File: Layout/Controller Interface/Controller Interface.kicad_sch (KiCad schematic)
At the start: 19 parts, among them J1 Conn_01x05_Socket, J2 Conn_01x05_Socket, J3 Conn_01x05_Socket, J4 Conn_01x05_Socket, Q1 FFB3904, Q3 FFB3904, SW1 SW_Push, SW2 SW_Push, U1 NRF24L01_Breakout, U2 Pico, U3 LD1117V33

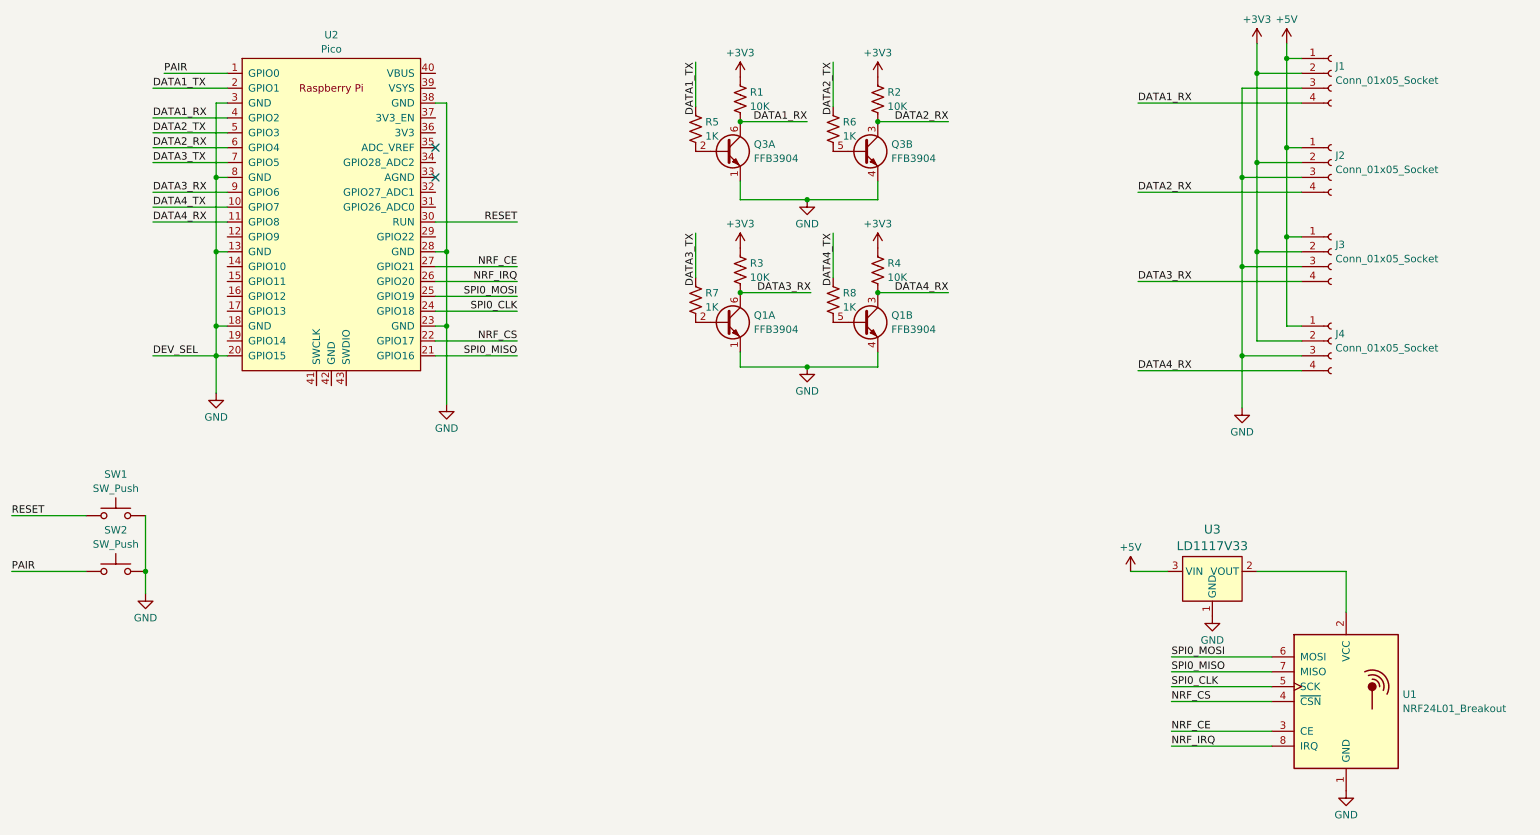
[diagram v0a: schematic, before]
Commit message: Refactor rx/tx PIO into single program
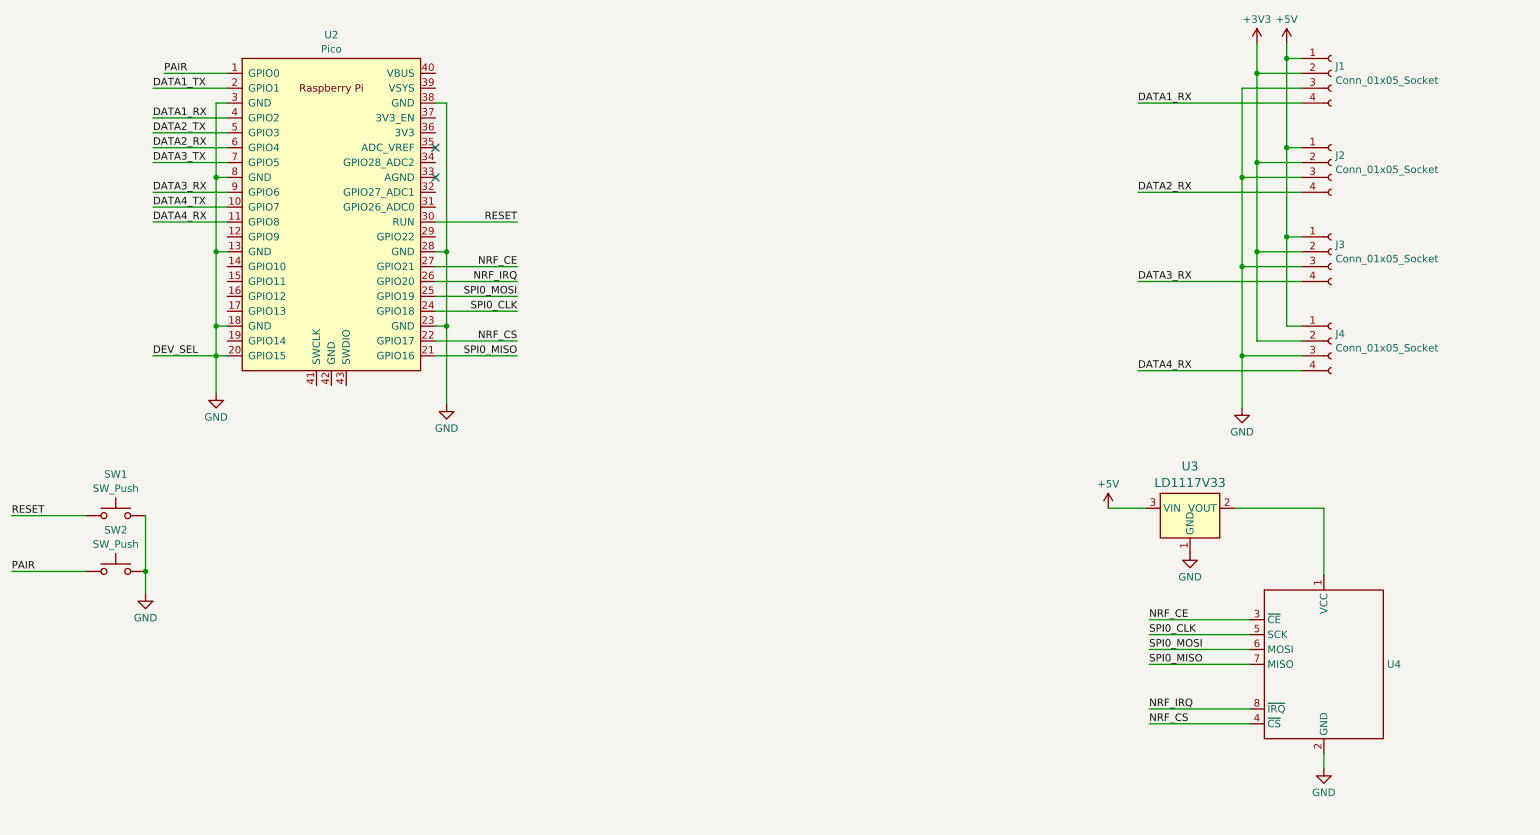
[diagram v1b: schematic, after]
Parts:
- removed Q1, Q3: FFB3904, Package_TO_SOT_SMD:SOT-363_SC-70-6, symbol Transistor_BJT:FFB3904
- removed R1, R2, R3, R4: 10K, symbol Device:R_US
- removed R5, R6, R7, R8: 1K, symbol Device:R_US
- removed U1: NRF24L01_Breakout, RF_Module:nRF24L01_Breakout, symbol RF:NRF24L01_Breakout
- added U4: ~, symbol RF:NRF24L01_Mini
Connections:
- net GND: now also U4.2 (GND)
- net NRF_CE: now also U4.3 (~{CE})
- net NRF_CS: now also U4.4 (~{CS})
- net NRF_IRQ: now also U4.8 (~{IRQ})
- net SPI0_CLK: now also U4.5 (SCK)
- net SPI0_MISO: now also U4.7 (MISO)
- net SPI0_MOSI: now also U4.6 (MOSI)
- net at U3.2 (VOUT): now also U4.1 (VCC)
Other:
- moved on the sheet: U3

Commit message: More work on the controller layout
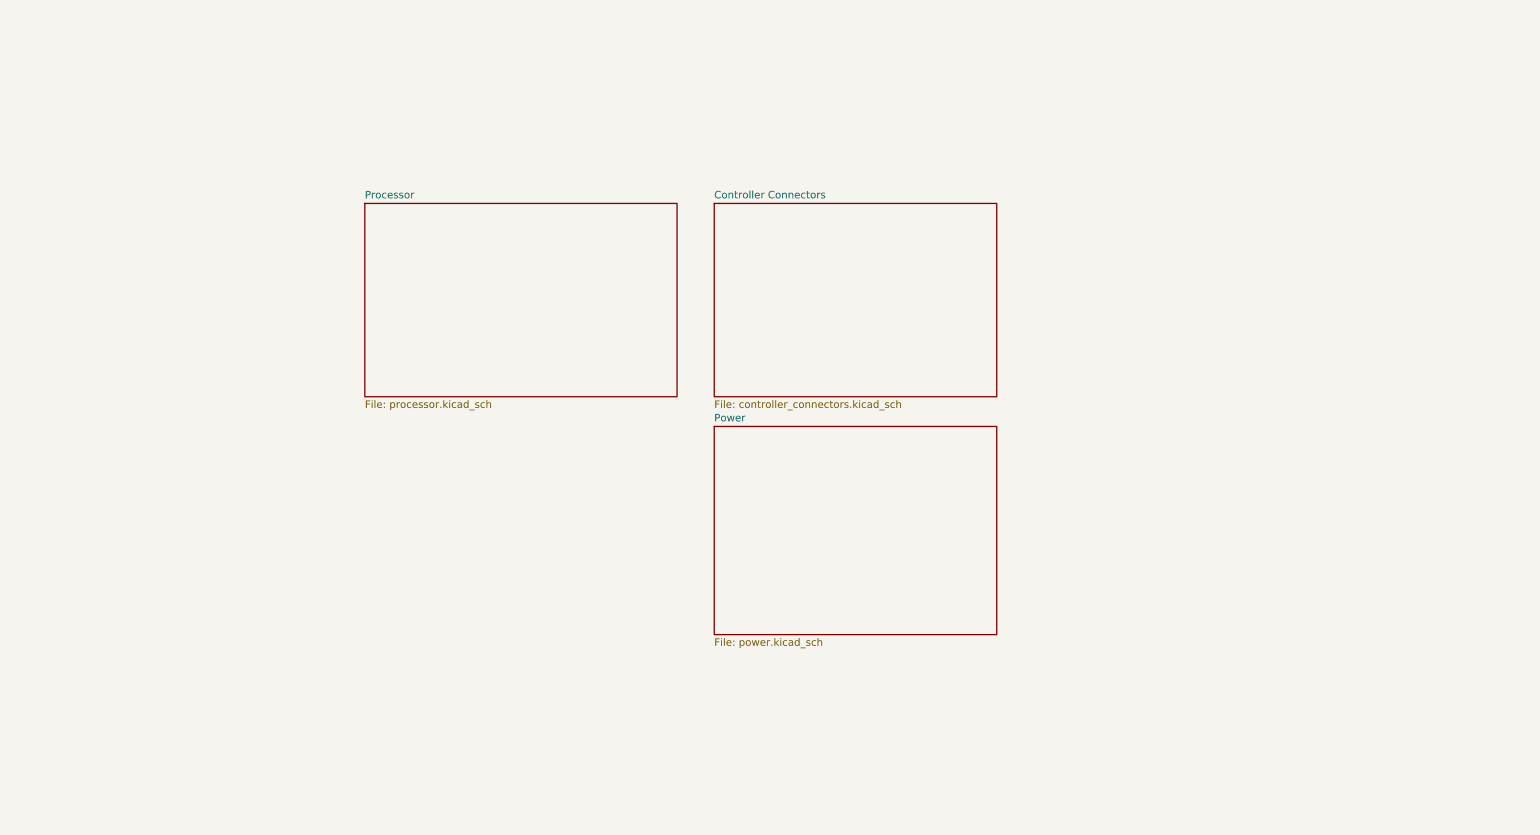
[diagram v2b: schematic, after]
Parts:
- removed J1, J2, J3, J4: Conn_01x05_Socket, symbol Connector:Conn_01x04_Socket
- removed SW1, SW2: SW_Push, symbol Switch:SW_Push
- removed U2: Pico, MCU_RaspberryPi_and_Boards:RPi_Pico_SMD_TH, symbol MCU_RaspberryPi_and_Boards:Pico
- removed U3: LD1117V33, digikey-footprints:TO-220-3, symbol dk_PMIC-Voltage-Regulators-Linear:LD1117V33
- removed U4: ~, symbol RF:NRF24L01_Mini
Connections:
- no-connect marks 2 -> 0
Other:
- added sheet Controller Connectors (controller_connectors.kicad_sch)
- added sheet Power (power.kicad_sch)
- added sheet Processor (processor.kicad_sch)

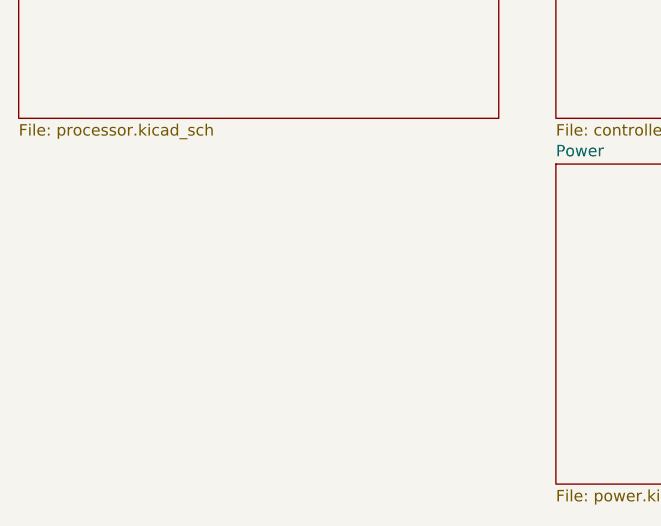
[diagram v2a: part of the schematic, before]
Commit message: Schematic updates
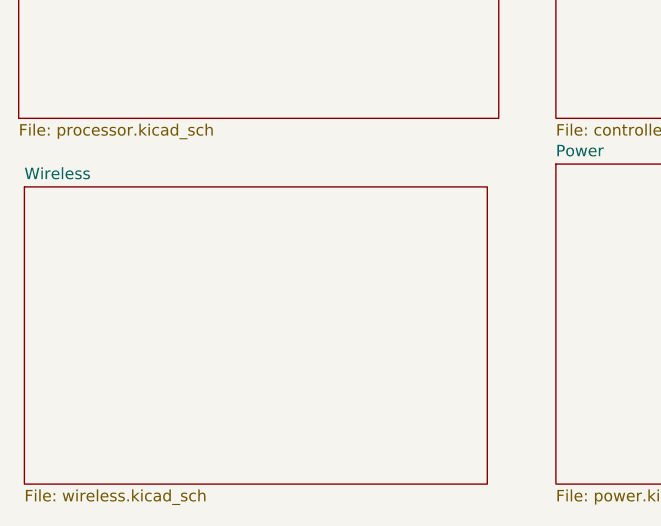
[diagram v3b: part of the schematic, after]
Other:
- added sheet Wireless (wireless.kicad_sch)
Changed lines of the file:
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@@
 (kicad_sch (version 20230121) (generator eeschema)
   (paper "A4")
+  (sheet (at 80.645 92.71) (size 51.435 33.02) (fields_autoplaced)
+    (stroke (width 0.1524) (type solid))
+    (fill (color 0 0 0 0.0000))
+    (property "Sheetname" "Wireless" (at 80.645 91.9984 0)
+      (effects (font (size 1.27 1.27)) (justify left bottom))
+    )
+    (property "Sheetfile" "wireless.kicad_sch" (at 80.645 126.3146 0)
+      (effects (font (size 1.27 1.27)) (justify left top))
+    )
+    (instances
+      (project "Controller Interface"
+        (path "/debf4462-021e-4805-bcd2-6130c1f65c4c" (page "5"))
+      )
+    )
+  )
   (sheet (at 139.7 90.17) (size 48.26 35.56) (fields_autoplaced)
     (stroke (width 0.1524) (type solid))
